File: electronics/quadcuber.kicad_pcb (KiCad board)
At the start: 4 copper layers, 144 x 112 mm, 200 parts, among them J1 9V regulated input, J10 EV3 R PINMAP HOLD, J11 EV3 L PINMAP HOLD, J12 EV3 F PINMAP HOLD, J13 EV3 B PINMAP HOLD, J2 UART GND TX RX, J20 R SERVO G + S, J21 L SERVO G + S, J22 F SERVO G + S, J23 B SERVO G + S, J3 RESET, J4 SWD VREF D G C, J5 USB-C data / BOOTSEL, Q1 CSD18540Q5B, U1 RP2040, U10 DRV8871DDAR, U11 DRV8871DDAR, U12 DRV8871DDAR, U13 DRV8871DDAR, U2 TPS54302DDCR, U20 SN74LVC2G17DBVR, U21 SN74LVC2G17DBVR, U22 SN74LVC2G17DBVR, U23 SN74LVC2G17DBVR, U3 TPS54302DDCR, U30 SN74AHCT1G125DBVR, U31 SN74AHCT1G125DBVR, U32 SN74AHCT1G125DBVR, U33 SN74AHCT1G125DBVR, U4 LM74700QDBVRQ1, U5 TLV75533PDBVR, U6 USBLC6-2SC6, U7 W25Q16RVCNJQ 2MiB, Y1 12MHz CL10pF

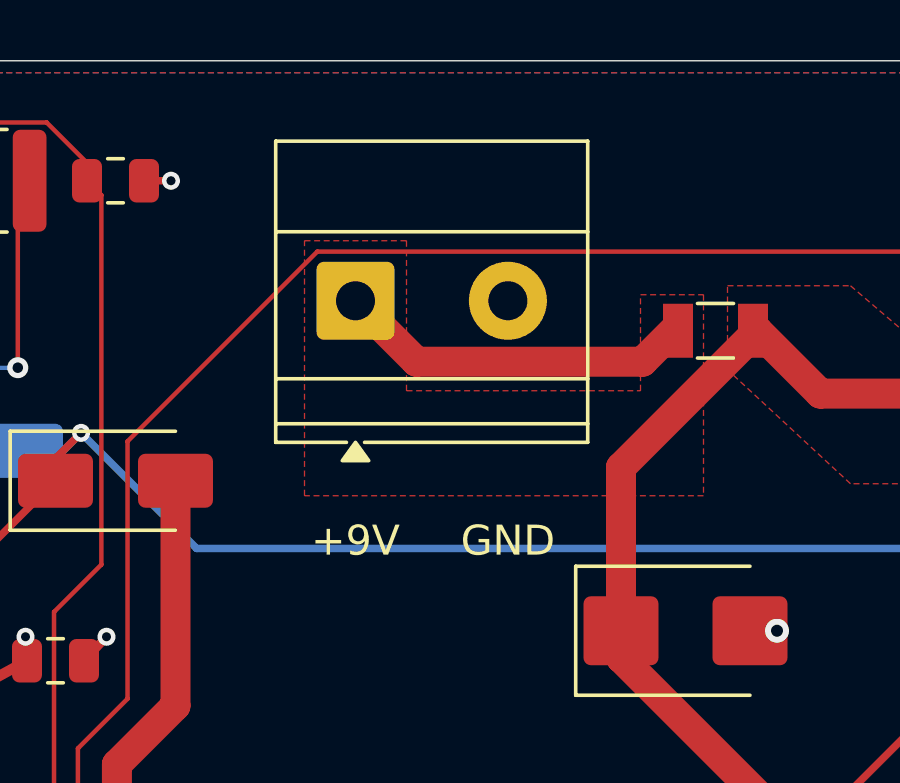
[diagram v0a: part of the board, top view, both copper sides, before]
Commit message: Replace J1 with center-positive RASPC722X DC input
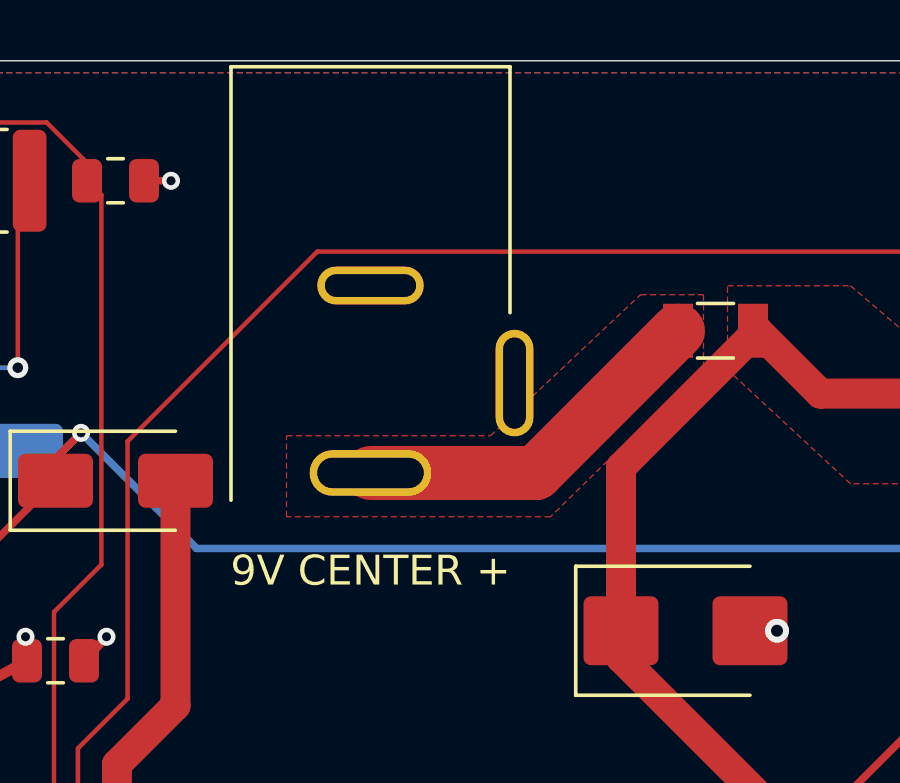
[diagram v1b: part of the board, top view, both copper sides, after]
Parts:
- J1: value 9V regulated input -> 9V DC center-positive; footprint Quadcuber:TerminalBlock_Phoenix_MKDS-1,5-2-5.08_1x02_P5.08mm_Horizontal -> Quadcuber:Jack_DC_Switchcraft_RASPC722X
- moved J1 8.02 mm to (95.5, 50.0)
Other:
- board text added: "9V CENTER +"
- board text removed: "+9V"
